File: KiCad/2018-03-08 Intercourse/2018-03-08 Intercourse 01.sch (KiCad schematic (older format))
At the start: 22 parts

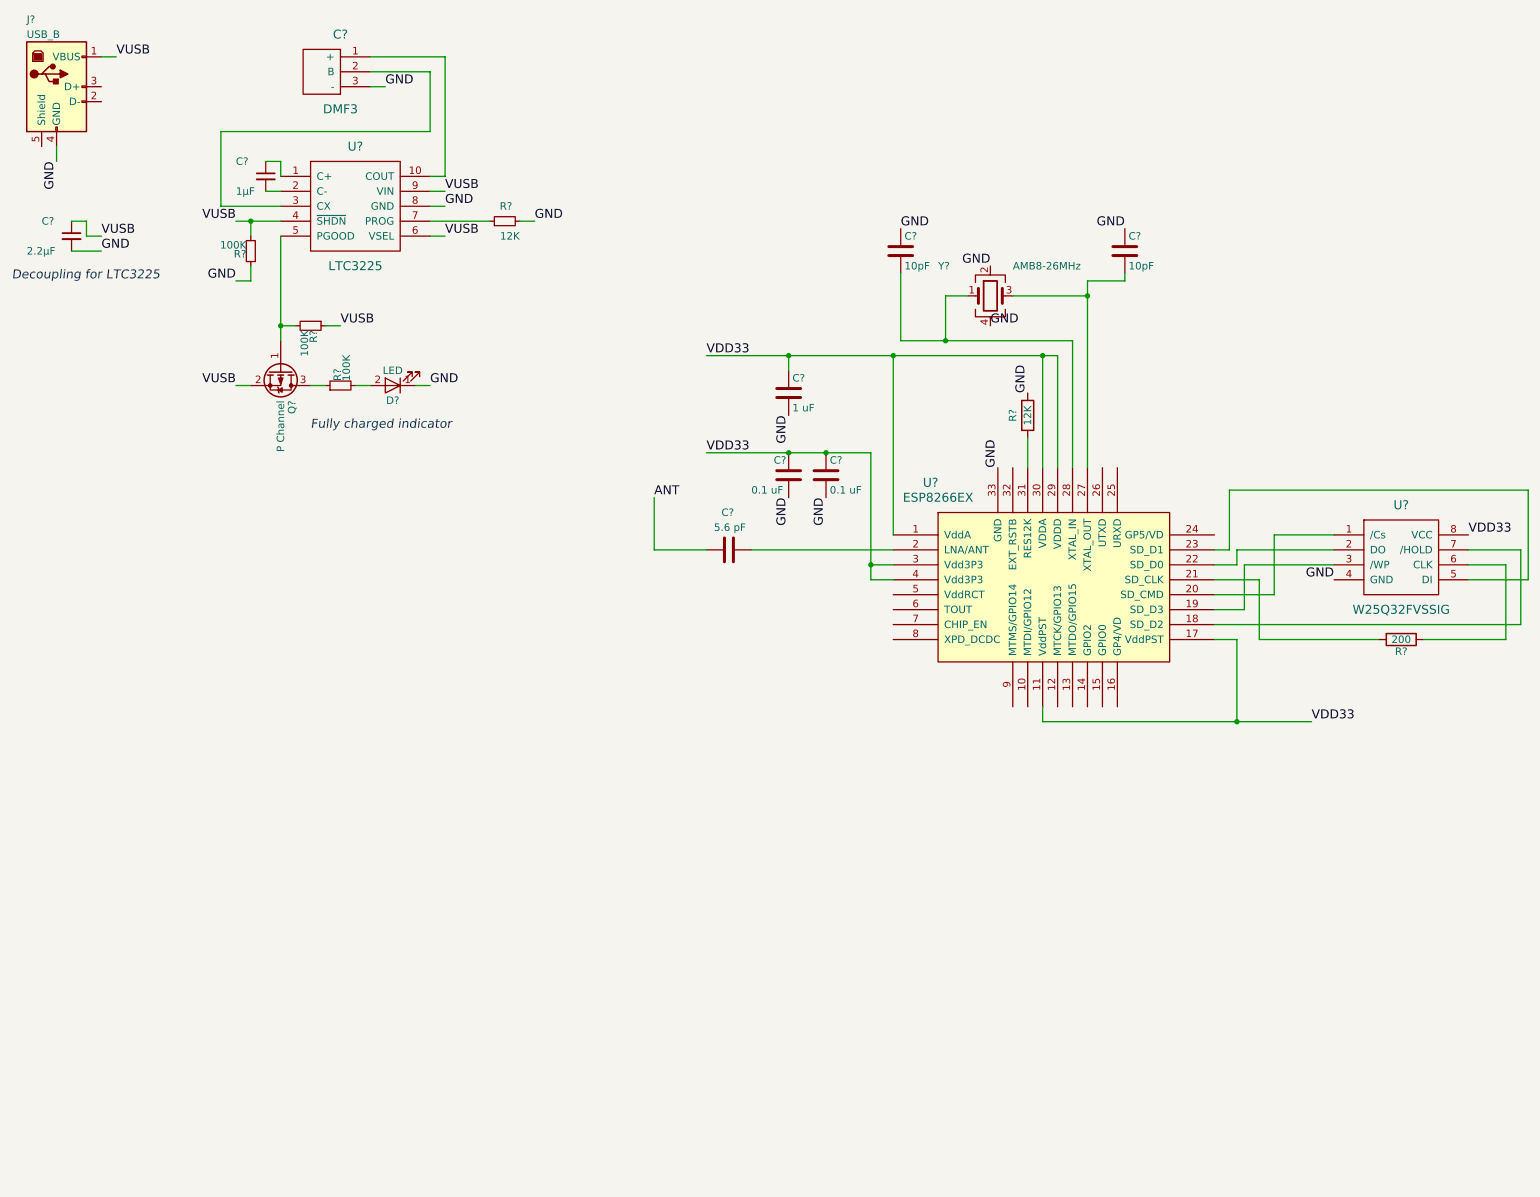
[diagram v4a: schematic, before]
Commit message: added booster circuit to schematic
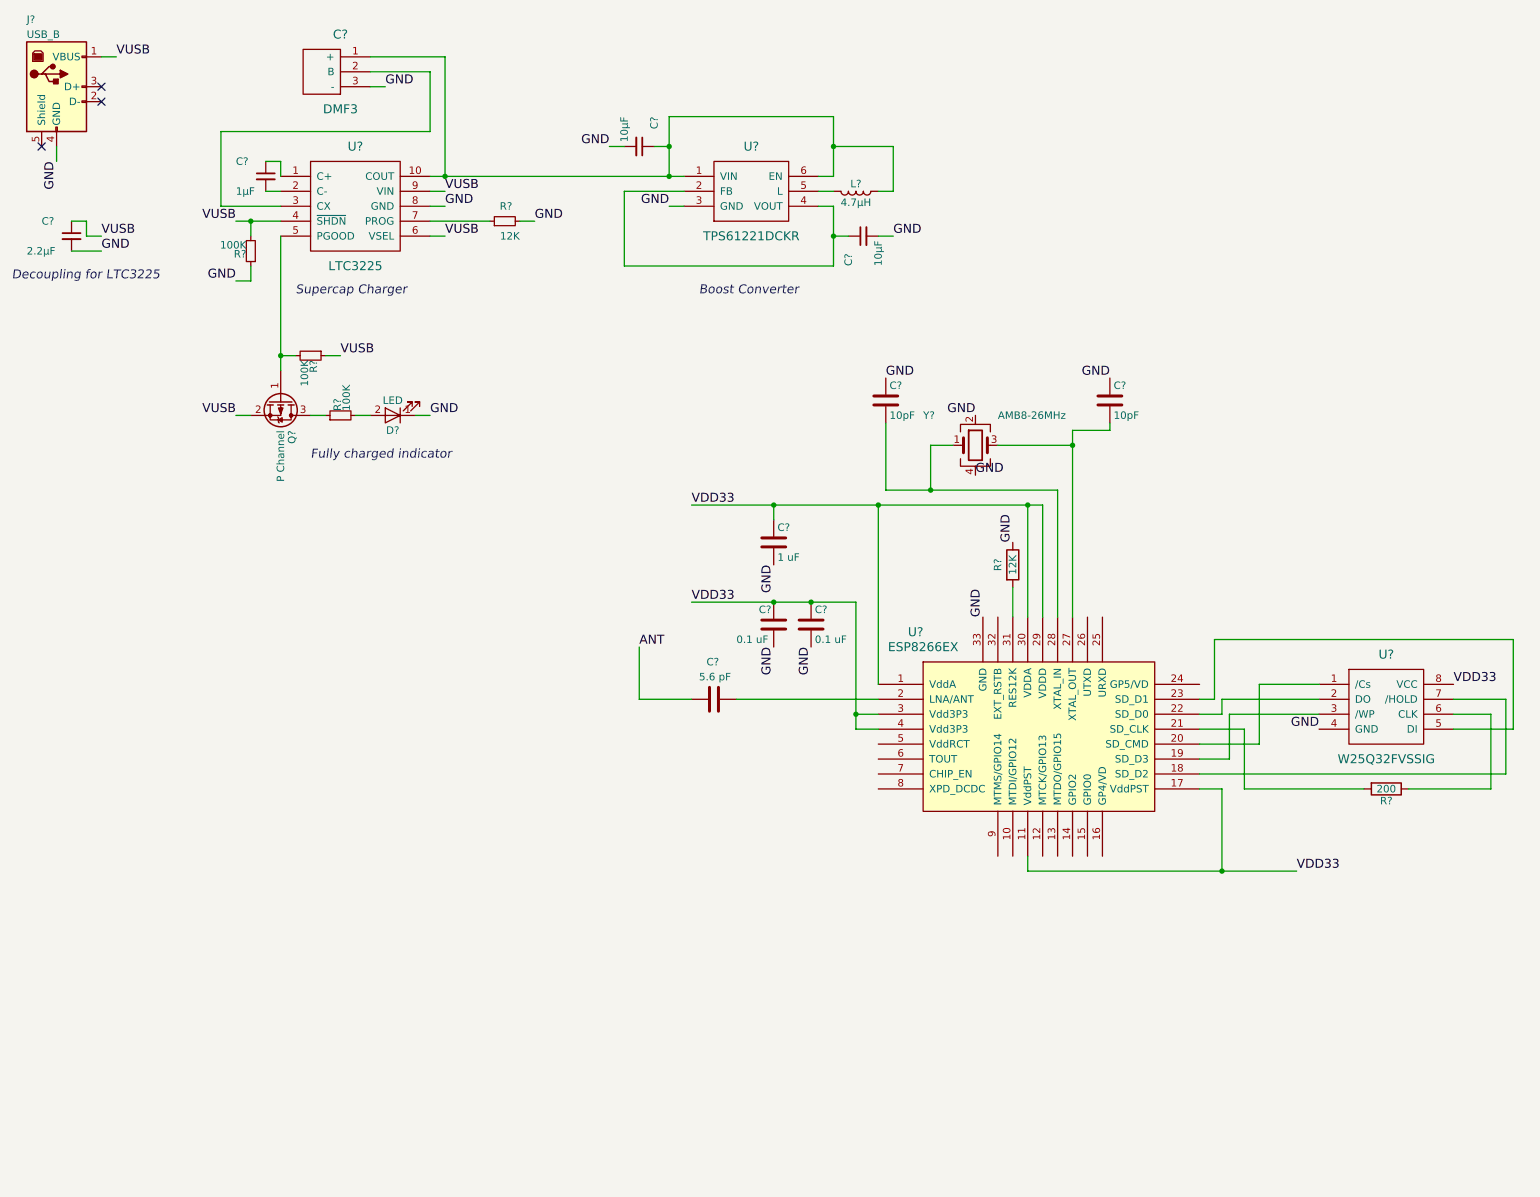
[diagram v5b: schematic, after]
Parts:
- added C? (x2): 10μF, symbol C_Small
- added L?: 4.7μH, symbol L
- added U?: TPS61221DCKR, symbol TPS61221DCKR
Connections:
- net GND: now also C?.2, C?.2, U?.3 (GND)
- net at C?.1 (+), U?.10 (COUT): now also C?.1, L?.1, U?.1 (VIN), U?.6 (EN)
- new net: C?.1, U?.2 (FB), U?.4 (VOUT)
- new net: L?.2, U?.5 (L)
- no-connect marks 0 -> 3
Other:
- note added: "Boost Converter"
- note added: "Supercap Charger"
- moved on the sheet: C?, D?, Q?, R?, U?, Y?

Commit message: plain schematic finished and beautified
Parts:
- removed C? (x2): 10pF, symbol C
- removed C?: 5.6 pF, symbol C
- removed C? (x2): 0.1 uF, symbol C
- removed C?: 1 uF, symbol C
- removed R?: 200, symbol R
- removed R?: 12K, symbol R
- removed U?: ESP8266EX, symbol ESP8266EX
- removed U?: W25Q32FVSSIG, symbol W25Q32FVSSIG
- removed Y?: AMB8-26MHz, symbol Crystal_GND24
- added C? (x2): 10μF, symbol C_Small
- added C?: 5.6pF, symbol C_Small
- added C? (x2): 10pF, symbol C_Small
- added C?: 2.2μF, symbol C_Small
- added R?: 12K, symbol R
- added R?: 200, symbol R
- added U?: ESP8266EX, symbol ESP8266EX
- added U?: W25Q32FVSSIG, symbol W25Q32FVSSIG
- added Y?: 26 MHz, symbol Crystal_GND24_Small
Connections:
- wire segments 101 -> 134
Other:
- note added: "Decoupling for\nVDDA, VDDD, VDDPST"
- note added: "Indicator LED for\nFully Loaded Cap"
- note added: "Micro USB Connector\nfor Power Supply"
- note added: "Microcontroller\nPeriphery"
- note added: "SPI Flash\nMemory"
- note added: "Supercap"
- note removed: "Fully charged indicator"
- moved on the sheet: C?, D?, J?, L?, Q?, R?, U?

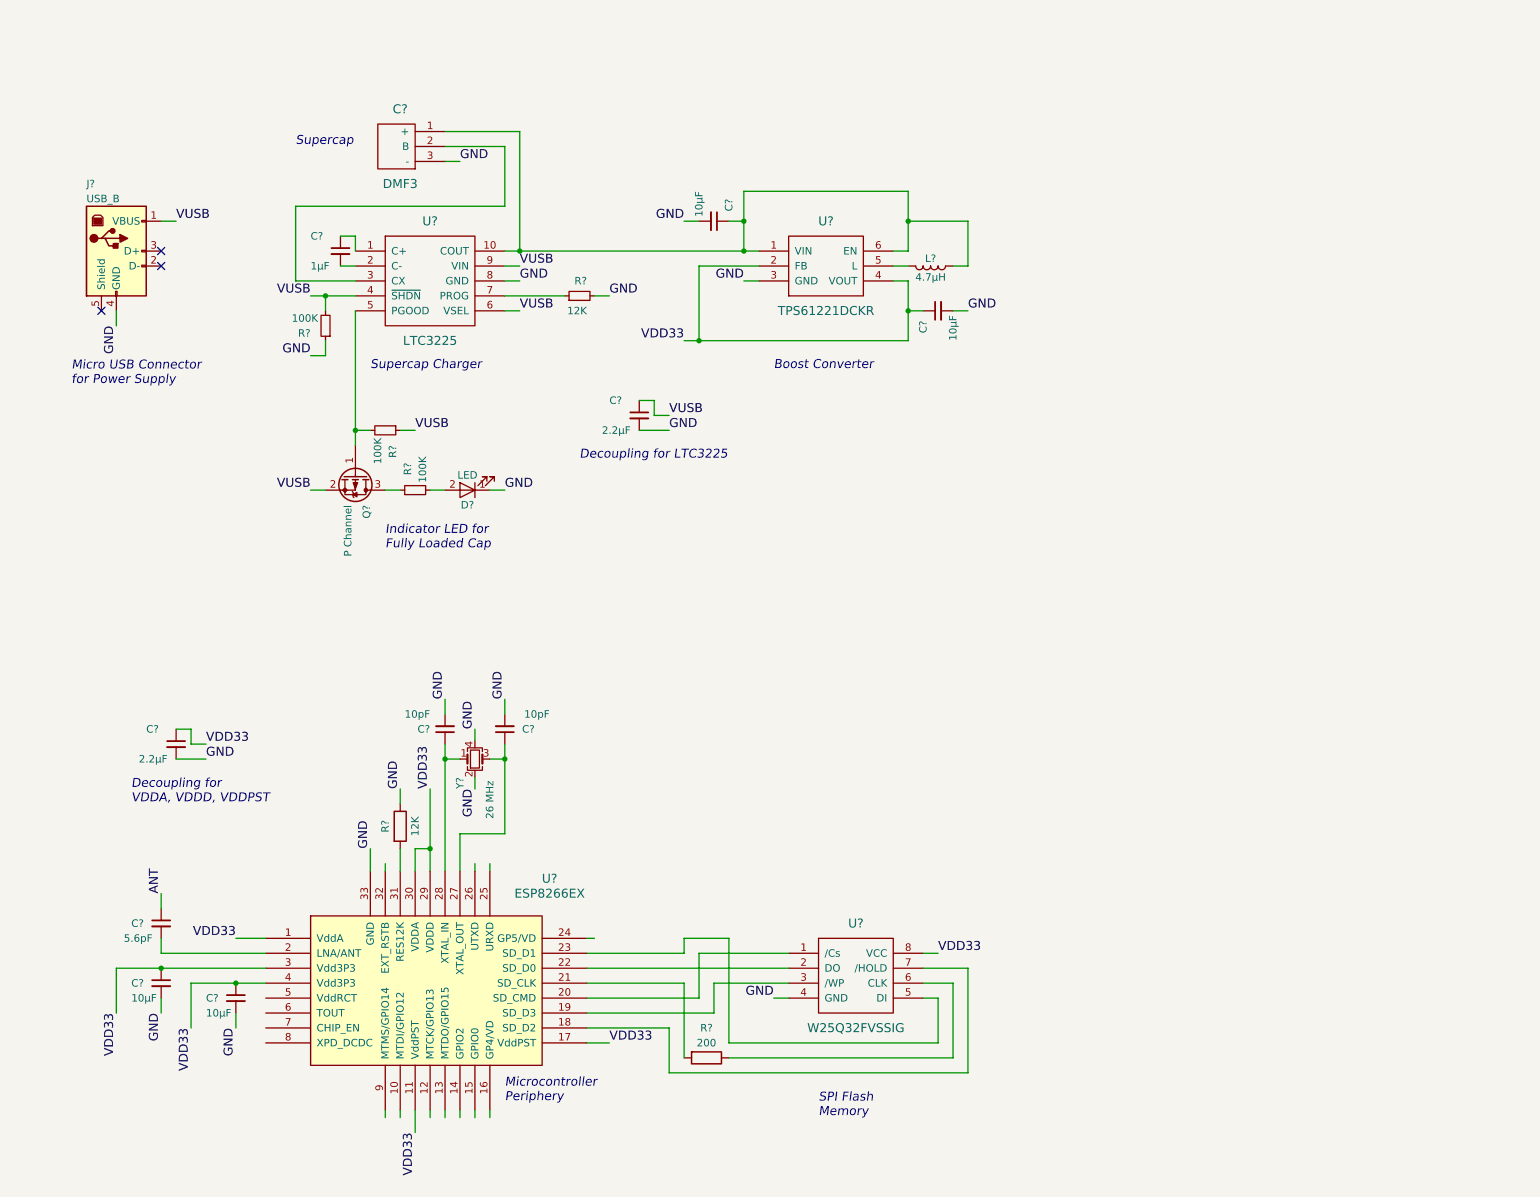
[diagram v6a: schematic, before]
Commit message: started adding dev and conn pins
not complete
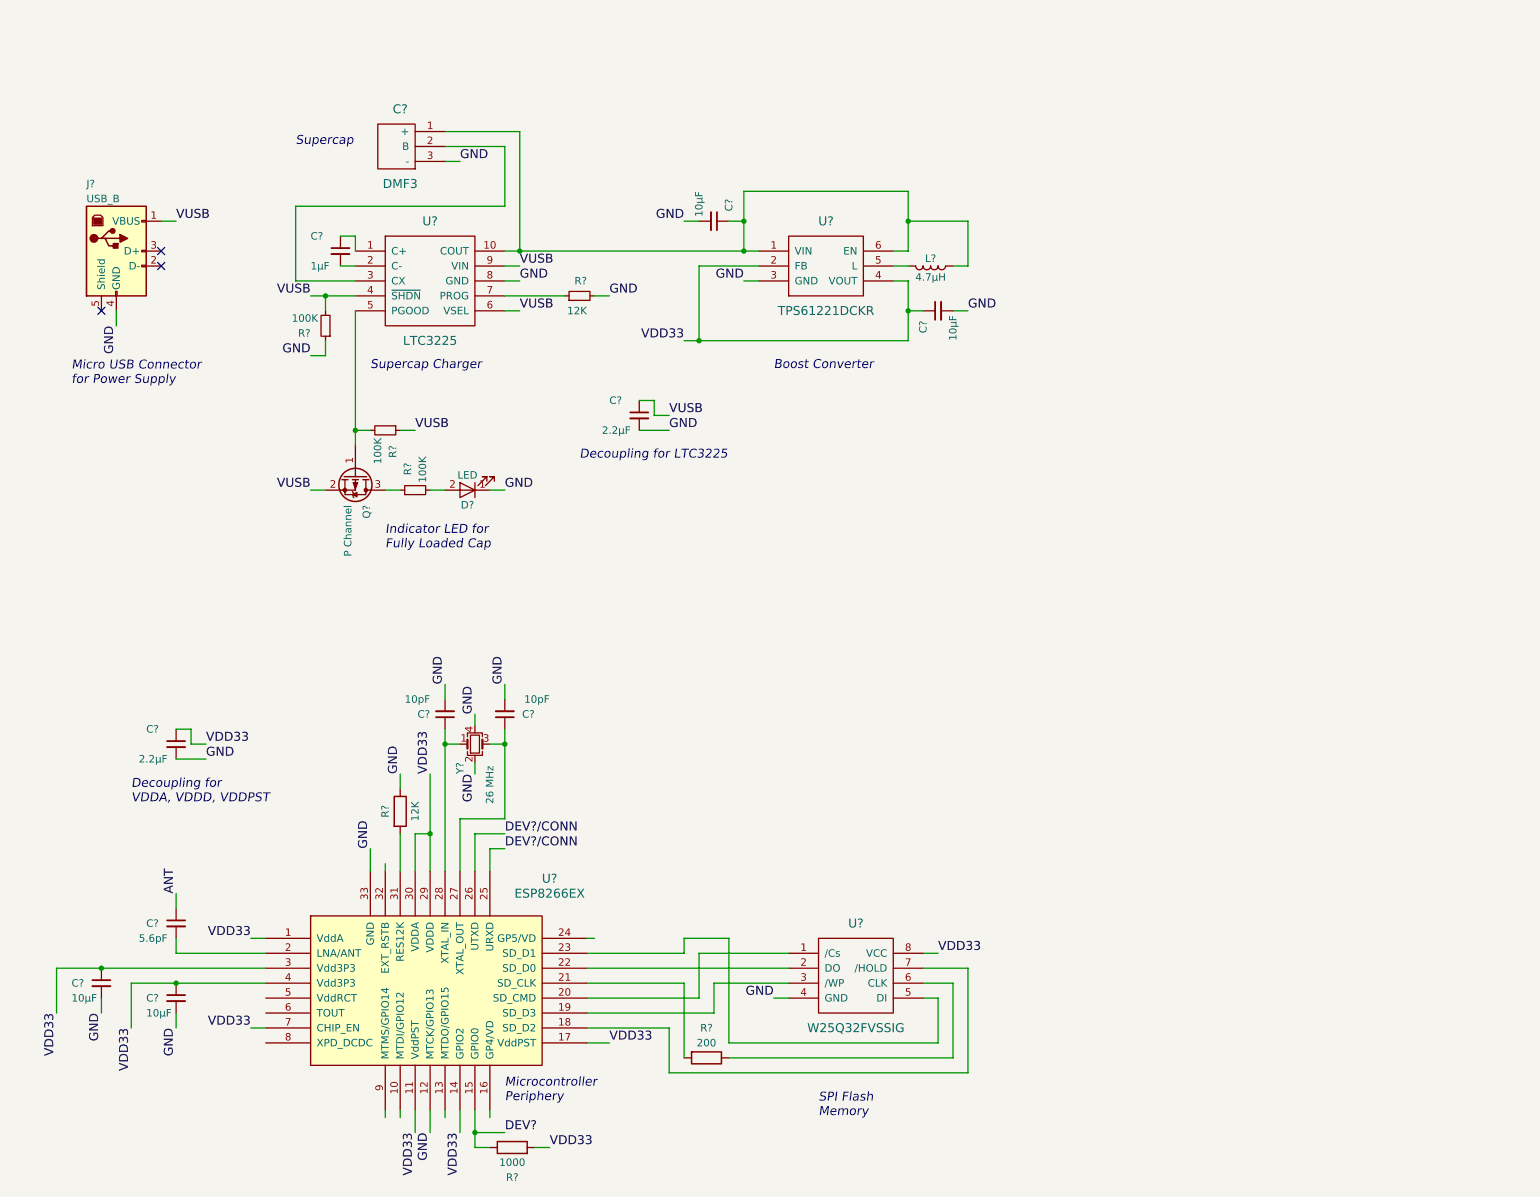
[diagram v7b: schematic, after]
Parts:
- added R?: 1000, symbol R
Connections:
- net labels added: DEV?, DEV?/CONN
- wire segments 134 -> 127
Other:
- moved on the sheet: C?, R?, Y?
